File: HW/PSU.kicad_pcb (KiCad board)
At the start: 2 copper layers, 10 parts, among them J1 USB-MINI, J2 USB_2, U1 MCP1642D-ADJ

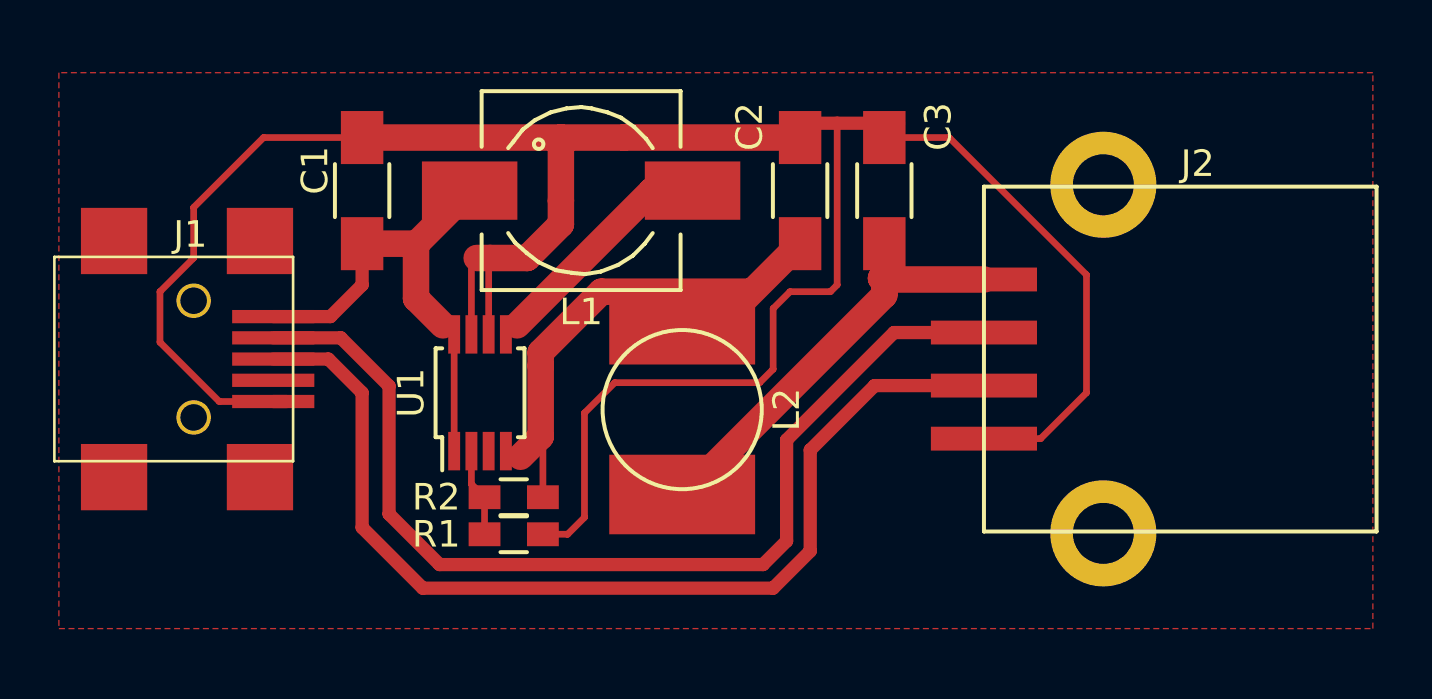
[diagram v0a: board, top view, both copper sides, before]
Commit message: PCB Errors corrected, some component size tweak.
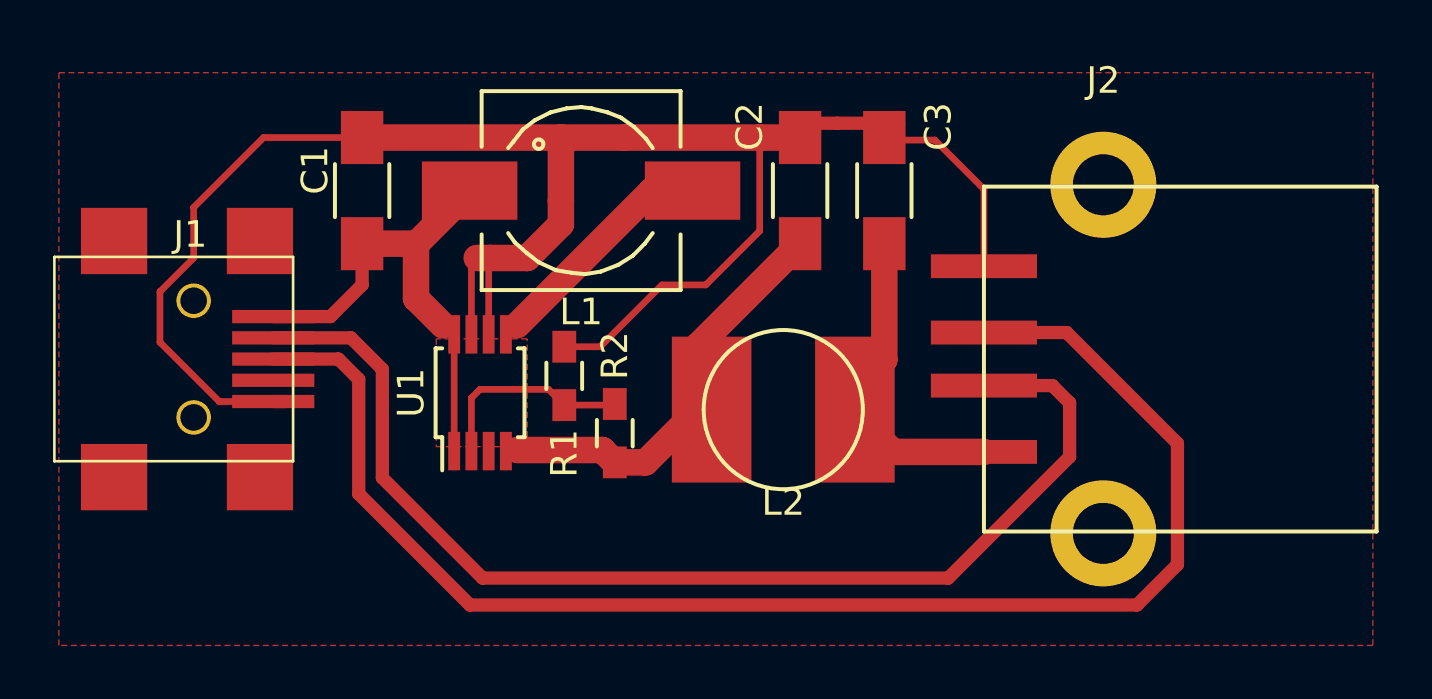
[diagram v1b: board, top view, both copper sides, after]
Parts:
- moved R1 6.27 mm to (52.1, 38.1), turned to 90 degrees
- moved R2 4.51 mm to (54.0, 40.3), turned to 270 degrees
- moved L2 3.81 mm to (60.3, 39.4), turned to 0 degrees
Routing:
- net GND: track 95.8 -> 72.4 mm
- net Net-(J1-Pad3): track 38.7 -> 54.7 mm
- net Net-(C2-Pad1): track 21.7 -> 16.1 mm
- net VCC: track 16.7 -> 11.9 mm
- net Net-(J1-Pad2): track 39.0 -> 43.6 mm
- net Net-(R1-Pad1): track 3.34 -> 7.86 mm

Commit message: Changed the polarity of the USB Connector
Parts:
- R1: value 309K -> 470K
- R2: value 976K -> 1,5M
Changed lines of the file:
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@@
-(kicad_pcb (version 4) (host pcbnew "(after 2015-mar-04 BZR unknown)-product")
+(kicad_pcb (version 4) (host pcbnew "(2015-06-16 BZR 5762, Git d3b3131)-product")
   (general
     (links 21)
     (no_connects 0)
-    (area 32.546289 25.786 83.019001 48.994)
+    (area 0 0 0 0)
     (thickness 1.6)
     (drawings 0)
@@
       (effects (font (size 1 1) (thickness 0.15)))
     )
-    (fp_text value 309K (at 0 0 90) (layer F.SilkS) hide
+    (fp_text value 470K (at 0 0 90) (layer F.SilkS) hide
       (effects (font (size 0.5 0.5) (thickness 0.1)))
     )
@@
       (effects (font (size 1 1) (thickness 0.15)))
     )
-    (fp_text value 976K (at 0 0 270) (layer F.SilkS) hide
+    (fp_text value 1,5M (at 0 0 270) (layer F.SilkS) hide
       (effects (font (size 0.5 0.5) (thickness 0.1)))
     )
@@
       (effects (font (size 1 1) (thickness 0.15)))
     )
-    (fp_text value MCP1642D-ADJ (at 0 2.6 90) (layer F.SilkS) hide
+    (fp_text value MCP1642D-ADJ (at -3.81 1.27 180) (layer F.SilkS) hide
       (effects (font (size 0.5 0.5) (thickness 0.1)))
     )
@@
       (effects (font (size 1 1) (thickness 0.15)))
     )
-    (fp_text value USB_2 (at 0 -10.5 180) (layer F.Fab)
+    (fp_text value USB_2 (at 0 -10.5 180) (layer F.Fab) hide
       (effects (font (size 1 1) (thickness 0.15)))
     )
@@
       (effects (font (size 1 1) (thickness 0.15)))
     )
-    (fp_text value 1uH (at 0 -3.6) (layer F.Fab)
-      (effects (font (size 1 1) (thickness 0.15)))
-    )
+    (fp_text value 1uH (at 0 -3.6) (layer F.Fab) hide
+      (effects (font (size 1 1) (thickness 0.15)))
+    )
